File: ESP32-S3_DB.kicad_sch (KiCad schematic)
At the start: 0 parts

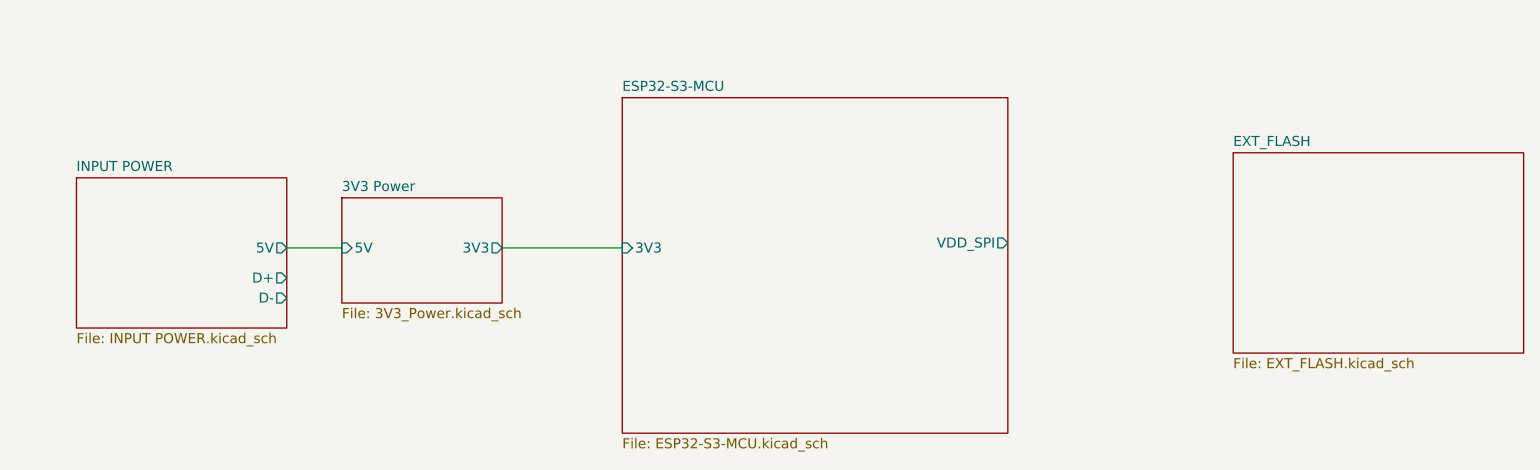
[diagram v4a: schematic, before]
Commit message: Added USB-To-UART Converter
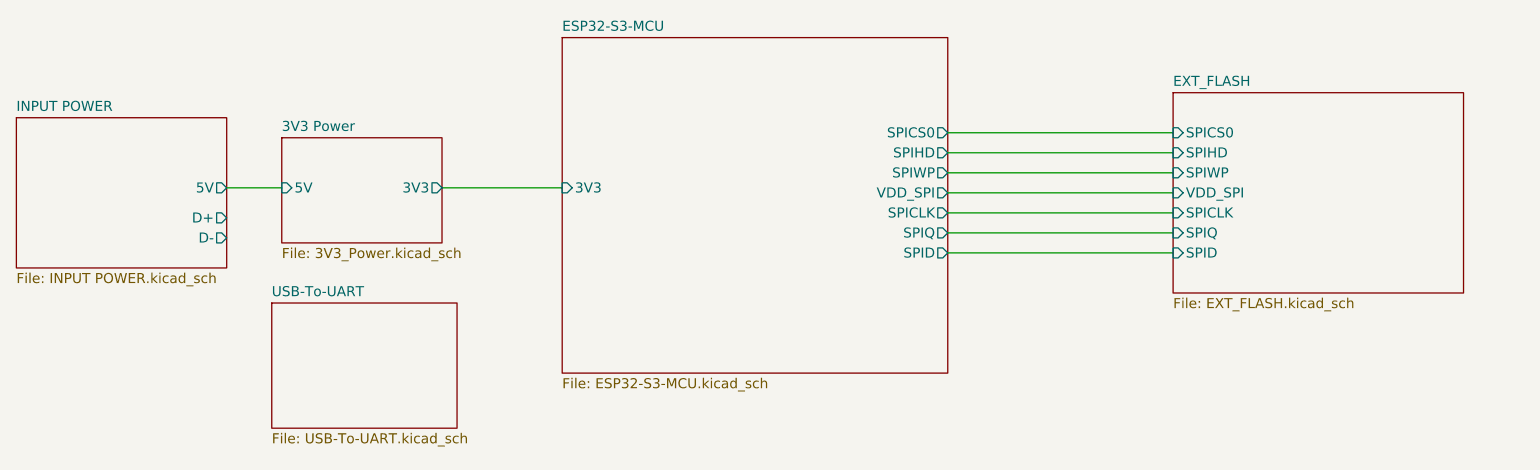
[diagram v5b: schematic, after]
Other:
- added sheet USB-To-UART (USB-To-UART.kicad_sch)
- sheet ESP32-S3-MCU ports: added SPICLK, SPICS0, SPID, SPIHD, SPIQ, SPIWP; removed none
- sheet EXT_FLASH ports: added SPICLK, SPICS0, SPID, SPIHD, SPIQ, SPIWP, VDD_SPI; removed none
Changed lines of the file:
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@@
 (kicad_sch (version 20230121) (generator eeschema)
   (paper "A4")
-  (wire (pts (xy 90.17 96.52) (xy 97.155 96.52))
+  (wire (pts (xy 173.99 97.155) (xy 202.565 97.155))
     (stroke (width 0) (type default))
   )
-  (wire (pts (xy 117.475 96.52) (xy 132.715 96.52))
+  (wire (pts (xy 173.99 92.075) (xy 202.565 92.075))
     (stroke (width 0) (type default))
   )
-  (sheet (at 210.185 84.455) (size 36.83 25.4) (fields_autoplaced)
+  (wire (pts (xy 173.99 94.615) (xy 202.565 94.615))
+    (stroke (width 0) (type default))
+  )
+  (wire (pts (xy 173.99 86.995) (xy 202.565 86.995))
+    (stroke (width 0) (type default))
+  )
+  (wire (pts (xy 173.99 89.535) (xy 202.565 89.535))
+    (stroke (width 0) (type default))
+  )
+  (wire (pts (xy 173.99 84.455) (xy 202.565 84.455))
+    (stroke (width 0) (type default))
+  )
+  (wire (pts (xy 82.55 88.9) (xy 89.535 88.9))
+    (stroke (width 0) (type default))
+  )
+  (wire (pts (xy 173.99 81.915) (xy 202.565 81.915))
+    (stroke (width 0) (type default))
+  )
+  (wire (pts (xy 109.855 88.9) (xy 125.095 88.9))
+    (stroke (width 0) (type default))
+  )
+  (sheet (at 202.565 76.835) (size 36.83 25.4) (fields_autoplaced)
     (stroke (width 0.1524) (type solid))
     (fill (color 255 255 194 1.0000))
-    (property "Sheetname" "EXT_FLASH" (at 210.185 83.7434 0)
+    (property "Sheetname" "EXT_FLASH" (at 202.565 76.1234 0)
       (effects (font (size 1.27 1.27)) (justify left bottom))
     )
-    (property "Sheetfile" "EXT_FLASH.kicad_sch" (at 210.185 110.4396 0)
+    (property "Sheetfile" "EXT_FLASH.kicad_sch" (at 202.565 102.8196 0)
       (effects (font (size 1.27 1.27)) (justify left top))
+    )
+    (pin "SPIHD" input (at 202.565 84.455 180)
+      (effects (font (size 1.27 1.27)) (justify left))
+    )
+    (pin "SPIWP" input (at 202.565 86.995 180)
+      (effects (font (size 1.27 1.27)) (justify left))
+    )
+    (pin "VDD_SPI" input (at 202.565 89.535 180)
+      (effects (font (size 1.27 1.27)) (justify left))
+    )
+    (pin "SPIQ" input (at 202.565 94.615 180)
+      (effects (font (size 1.27 1.27)) (justify left))
+    )
+    (pin "SPICLK" input (at 202.565 92.075 180)
+      (effects (font (size 1.27 1.27)) (justify left))
+    )
+    (pin "SPICS0" input (at 202.565 81.915 180)
+      (effects (font (size 1.27 1.27)) (justify left))
+    )
+    (pin "SPID" input (at 202.565 97.155 180)
+      (effects (font (size 1.27 1.27)) (justify left))
     )
     (instances
@@
     )
   )
-  (sheet (at 63.5 87.63) (size 26.67 19.05) (fields_autoplaced)
+  (sheet (at 55.88 80.01) (size 26.67 19.05) (fields_autoplaced)
     (stroke (width 0.1524) (type solid))
     (fill (color 255 255 194 1.0000))
-    (property "Sheetname" "INPUT POWER" (at 63.5 86.9184 0)
+    (property "Sheetname" "INPUT POWER" (at 55.88 79.2984 0)
       (effects (font (size 1.27 1.27)) (justify left bottom))
     )
-    (property "Sheetfile" "INPUT POWER.kicad_sch" (at 63.5 107.2646 0)
+    (property "Sheetfile" "INPUT POWER.kicad_sch" (at 55.88 99.6446 0)
       (effects (font (size 1.27 1.27)) (justify left top))
     )
-    (pin "D-" output (at 90.17 102.87 0)
+    (pin "D-" output (at 82.55 95.25 0)
       (effects (font (size 1.27 1.27)) (justify right))
     )
-    (pin "D+" output (at 90.17 100.33 0)
+    (pin "D+" output (at 82.55 92.71 0)
       (effects (font (size 1.27 1.27)) (justify right))
     )
-    (pin "5V" output (at 90.17 96.52 0)
+    (pin "5V" output (at 82.55 88.9 0)
       (effects (font (size 1.27 1.27)) (justify right))
     )
@@
     )
   )
-  (sheet (at 132.715 77.47) (size 48.895 42.545) (fields_autoplaced)
+  (sheet (at 88.265 103.505) (size 23.495 15.875) (fields_autoplaced)
     (stroke (width 0.1524) (type solid))
     (fill (color 255 255 194 1.0000))
-    (property "Sheetname" "ESP32-S3-MCU" (at 132.715 76.7584 0)
+    (property "Sheetname" "USB-To-UART" (at 88.265 102.7934 0)
       (effects (font (size 1.27 1.27)) (justify left bottom))
     )
-    (property "Sheetfile" "ESP32-S3-MCU.kicad_sch" (at 132.715 120.5996 0)
+    (property "Sheetfile" "USB-To-UART.kicad_sch" (at 88.265 119.9646 0)
       (effects (font (size 1.27 1.27)) (justify left top))
     )
-    (pin "3V3" input (at 132.715 96.52 180)
+    (instances
+      (project "ESP32-S3_DB"
+        (path "/b7fc4bd3-c219-4455-832b-8d795385dcf1" (page "6"))
+      )
+    )
+  )
+  (sheet (at 125.095 69.85) (size 48.895 42.545) (fields_autoplaced)
+    (stroke (width 0.1524) (type solid))
+    (fill (color 255 255 194 1.0000))
+    (property "Sheetname" "ESP32-S3-MCU" (at 125.095 69.1384 0)
+      (effects (font (size 1.27 1.27)) (justify left bottom))
+    )
+    (property "Sheetfile" "ESP32-S3-MCU.kicad_sch" (at 125.095 112.9796 0)
+      (effects (font (size 1.27 1.27)) (justify left top))
+    )
+    (pin "3V3" input (at 125.095 88.9 180)
       (effects (font (size 1.27 1.27)) (justify left))
     )
-    (pin "VDD_SPI" output (at 181.61 95.885 0)
+    (pin "VDD_SPI" output (at 173.99 89.535 0)
+      (effects (font (size 1.27 1.27)) (justify right))
+    )
+    (pin "SPIWP" output (at 173.99 86.995 0)
+      (effects (font (size 1.27 1.27)) (justify right))
+    )
+    (pin "SPIHD" output (at 173.99 84.455 0)
+      (effects (font (size 1.27 1.27)) (justify right))
+    )
+    (pin "SPICS0" output (at 173.99 81.915 0)
+      (effects (font (size 1.27 1.27)) (justify right))
+    )
+    (pin "SPICLK" output (at 173.99 92.075 0)
+      (effects (font (size 1.27 1.27)) (justify right))
+    )
+    (pin "SPIQ" output (at 173.99 94.615 0)
+      (effects (font (size 1.27 1.27)) (justify right))
+    )
+    (pin "SPID" output (at 173.99 97.155 0)
       (effects (font (size 1.27 1.27)) (justify right))
     )
@@
     )
   )
-  (sheet (at 97.155 90.17) (size 20.32 13.335) (fields_autoplaced)
+  (sheet (at 89.535 82.55) (size 20.32 13.335) (fields_autoplaced)
     (stroke (width 0.1524) (type solid))
     (fill (color 255 255 194 1.0000))
-    (property "Sheetname" "3V3 Power" (at 97.155 89.4584 0)
+    (property "Sheetname" "3V3 Power" (at 89.535 81.8384 0)
       (effects (font (size 1.27 1.27)) (justify left bottom))
     )
-    (property "Sheetfile" "3V3_Power.kicad_sch" (at 97.155 104.0896 0)
+    (property "Sheetfile" "3V3_Power.kicad_sch" (at 89.535 96.4696 0)
       (effects (font (size 1.27 1.27)) (justify left top))
     )
-    (pin "3V3" output (at 117.475 96.52 0)
+    (pin "3V3" output (at 109.855 88.9 0)
       (effects (font (size 1.27 1.27)) (justify right))
     )
-    (pin "5V" input (at 97.155 96.52 180)
+    (pin "5V" input (at 89.535 88.9 180)
       (effects (font (size 1.27 1.27)) (justify left))
     )

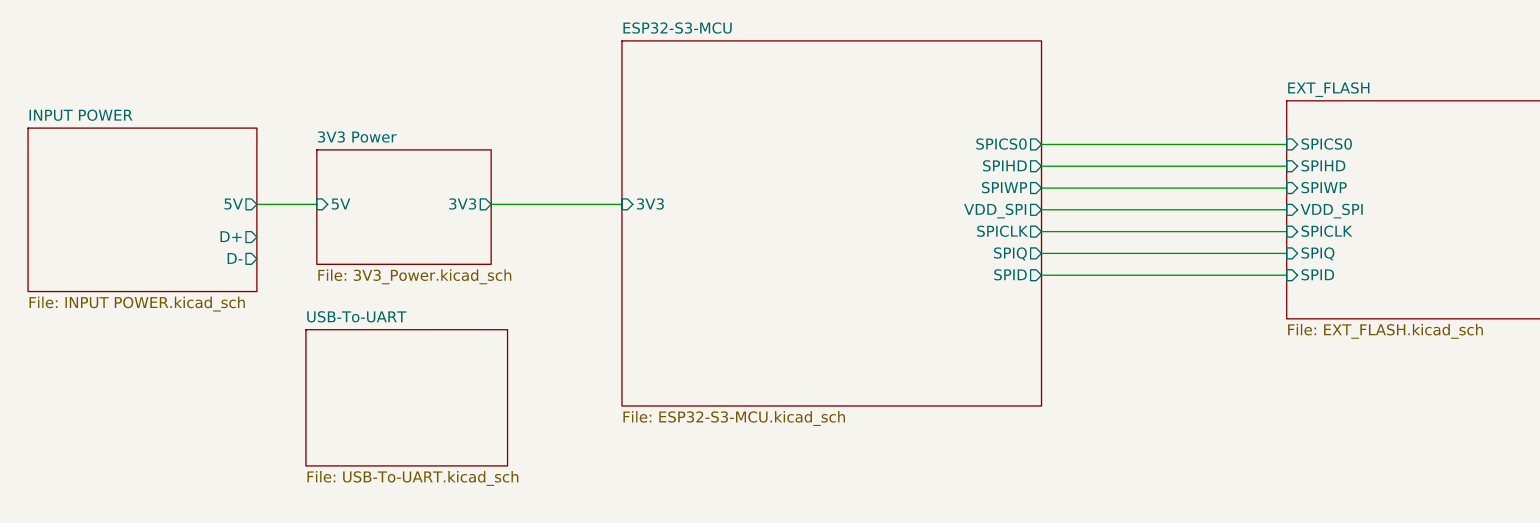
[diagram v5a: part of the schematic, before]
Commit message: Made USB-To-UART connections
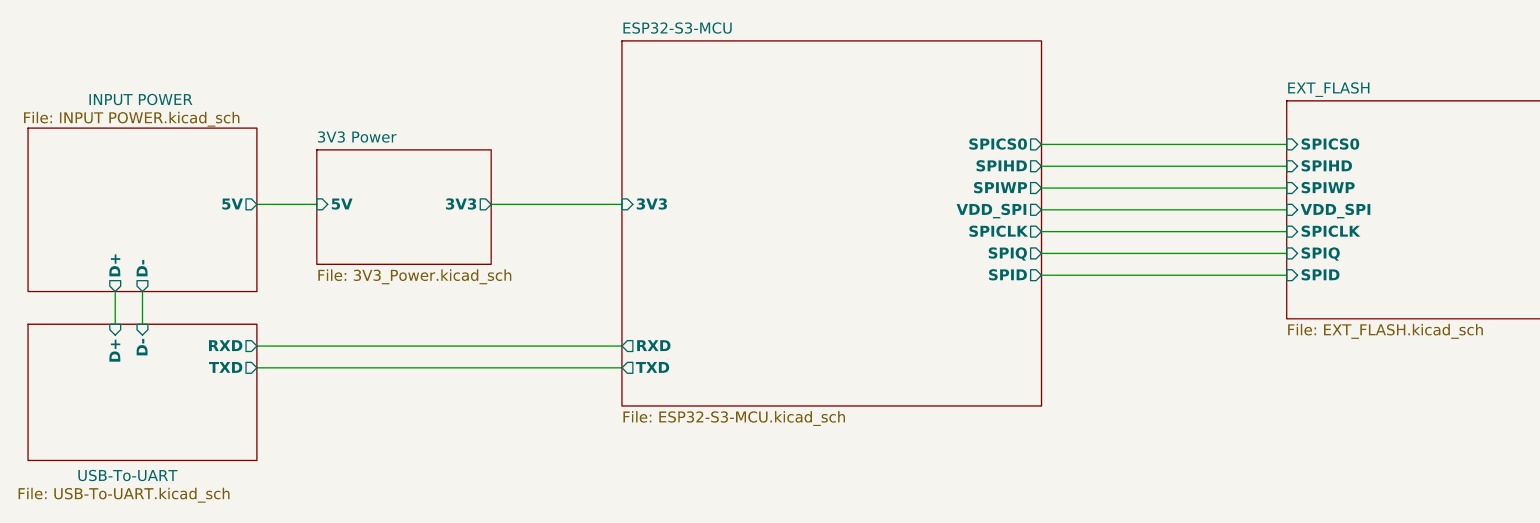
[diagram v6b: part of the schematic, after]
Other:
- sheet ESP32-S3-MCU ports: added RXD, TXD; removed none
- sheet USB-To-UART ports: added D+, D-, RXD, TXD; removed none
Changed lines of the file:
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@@
+    (stroke (width 0) (type default))
+  )
+  (wire (pts (xy 66.04 99.06) (xy 66.04 102.87))
+    (stroke (width 0) (type default))
+  )
+  (wire (pts (xy 69.215 99.06) (xy 69.215 102.87))
     (stroke (width 0) (type default))
   )
@@
     (stroke (width 0) (type default))
   )
+  (wire (pts (xy 82.55 105.41) (xy 125.095 105.41))
+    (stroke (width 0) (type default))
+  )
   (wire (pts (xy 173.99 81.915) (xy 202.565 81.915))
     (stroke (width 0) (type default))
@@
     (stroke (width 0) (type default))
   )
+  (wire (pts (xy 82.55 107.95) (xy 125.095 107.95))
+    (stroke (width 0) (type default))
+  )
   (sheet (at 202.565 76.835) (size 36.83 25.4) (fields_autoplaced)
-    (stroke (width 0.1524) (type solid))
+    (stroke (width 0.1524) (type solid) (color 0 0 0 1))
     (fill (color 255 255 194 1.0000))
     (property "Sheetname" "EXT_FLASH" (at 202.565 76.1234 0)
@@
     )
     (pin "SPIHD" input (at 202.565 84.455 180)
-      (effects (font (size 1.27 1.27)) (justify left))
+      (effects (font (size 1.27 1.27) (thickness 0.254) bold (color 0 0 255 1)) (justify left))
     )
     (pin "SPIWP" input (at 202.565 86.995 180)
-      (effects (font (size 1.27 1.27)) (justify left))
+      (effects (font (size 1.27 1.27) (thickness 0.254) bold (color 0 0 255 1)) (justify left))
     )
     (pin "VDD_SPI" input (at 202.565 89.535 180)
-      (effects (font (size 1.27 1.27)) (justify left))
+      (effects (font (size 1.27 1.27) (thickness 0.254) bold (color 0 0 255 1)) (justify left))
     )
     (pin "SPIQ" input (at 202.565 94.615 180)
-      (effects (font (size 1.27 1.27)) (justify left))
+      (effects (font (size 1.27 1.27) (thickness 0.254) bold (color 0 0 255 1)) (justify left))
     )
     (pin "SPICLK" input (at 202.565 92.075 180)
-      (effects (font (size 1.27 1.27)) (justify left))
+      (effects (font (size 1.27 1.27) (thickness 0.254) bold (color 0 0 255 1)) (justify left))
     )
     (pin "SPICS0" input (at 202.565 81.915 180)
-      (effects (font (size 1.27 1.27)) (justify left))
+      (effects (font (size 1.27 1.27) (thickness 0.254) bold (color 0 0 255 1)) (justify left))
     )
     (pin "SPID" input (at 202.565 97.155 180)
-      (effects (font (size 1.27 1.27)) (justify left))
+      (effects (font (size 1.27 1.27) (thickness 0.254) bold (color 0 0 255 1)) (justify left))
     )
     (instances
@@
     )
   )
-  (sheet (at 55.88 80.01) (size 26.67 19.05) (fields_autoplaced)
-    (stroke (width 0.1524) (type solid))
+  (sheet (at 55.88 80.01) (size 26.67 19.05)
+    (stroke (width 0.1524) (type solid) (color 0 0 0 1))
     (fill (color 255 255 194 1.0000))
-    (property "Sheetname" "INPUT POWER" (at 55.88 79.2984 0)
+    (property "Sheetname" "INPUT POWER" (at 62.865 77.47 0)
       (effects (font (size 1.27 1.27)) (justify left bottom))
     )
-    (property "Sheetfile" "INPUT POWER.kicad_sch" (at 55.88 99.6446 0)
+    (property "Sheetfile" "INPUT POWER.kicad_sch" (at 55.245 78.105 0)
       (effects (font (size 1.27 1.27)) (justify left top))
     )
-    (pin "D-" output (at 82.55 95.25 0)
-      (effects (font (size 1.27 1.27)) (justify right))
+    (pin "D-" output (at 69.215 99.06 270)
+      (effects (font (size 1.27 1.27) (thickness 0.254) bold (color 0 0 255 1)) (justify left))
     )
-    (pin "D+" output (at 82.55 92.71 0)
-      (effects (font (size 1.27 1.27)) (justify right))
+    (pin "D+" output (at 66.04 99.06 270)
+      (effects (font (size 1.27 1.27) (thickness 0.254) bold (color 0 0 255 1)) (justify left))
     )
     (pin "5V" output (at 82.55 88.9 0)
-      (effects (font (size 1.27 1.27)) (justify right))
+      (effects (font (size 1.27 1.27) (thickness 0.254) bold (color 255 0 0 1)) (justify right))
     )
     (instances
@@
     )
   )
-  (sheet (at 88.265 103.505) (size 23.495 15.875) (fields_autoplaced)
-    (stroke (width 0.1524) (type solid))
+  (sheet (at 55.88 102.87) (size 26.67 15.875)
+    (stroke (width 0.1524) (type solid) (color 0 0 0 1))
     (fill (color 255 255 194 1.0000))
-    (property "Sheetname" "USB-To-UART" (at 88.265 102.7934 0)
+    (property "Sheetname" "USB-To-UART" (at 61.595 121.285 0)
       (effects (font (size 1.27 1.27)) (justify left bottom))
     )
-    (property "Sheetfile" "USB-To-UART.kicad_sch" (at 88.265 119.9646 0)
+    (property "Sheetfile" "USB-To-UART.kicad_sch" (at 54.61 121.92 0)
       (effects (font (size 1.27 1.27)) (justify left top))
+    )
+    (pin "D+" input (at 66.04 102.87 90)
+      (effects (font (size 1.27 1.27) (thickness 0.254) bold (color 0 0 255 1)) (justify right))
+    )
+    (pin "D-" input (at 69.215 102.87 90)
+      (effects (font (size 1.27 1.27) (thickness 0.254) bold (color 0 0 255 1)) (justify right))
+    )
+    (pin "RXD" output (at 82.55 105.41 0)
+      (effects (font (size 1.27 1.27) (thickness 0.254) bold (color 0 0 255 1)) (justify right))
+    )
+    (pin "TXD" output (at 82.55 107.95 0)
+      (effects (font (size 1.27 1.27) (thickness 0.254) bold (color 0 0 255 1)) (justify right))
     )
     (instances
@@
   )
   (sheet (at 125.095 69.85) (size 48.895 42.545) (fields_autoplaced)
-    (stroke (width 0.1524) (type solid))
+    (stroke (width 0.1524) (type solid) (color 0 0 0 1))
     (fill (color 255 255 194 1.0000))
     (property "Sheetname" "ESP32-S3-MCU" (at 125.095 69.1384 0)
@@
     )
     (pin "3V3" input (at 125.095 88.9 180)
-      (effects (font (size 1.27 1.27)) (justify left))
+      (effects (font (size 1.27 1.27) (thickness 0.254) bold (color 255 0 0 1)) (justify left))
     )
     (pin "VDD_SPI" output (at 173.99 89.535 0)
-      (effects (font (size 1.27 1.27)) (justify right))
+      (effects (font (size 1.27 1.27) (thickness 0.254) bold (color 0 0 255 1)) (justify right))
     )
     (pin "SPIWP" output (at 173.99 86.995 0)
-      (effects (font (size 1.27 1.27)) (justify right))
+      (effects (font (size 1.27 1.27) (thickness 0.254) bold (color 0 0 255 1)) (justify right))
     )
     (pin "SPIHD" output (at 173.99 84.455 0)
-      (effects (font (size 1.27 1.27)) (justify right))
+      (effects (font (size 1.27 1.27) (thickness 0.254) bold (color 0 0 255 1)) (justify right))
     )
     (pin "SPICS0" output (at 173.99 81.915 0)
-      (effects (font (size 1.27 1.27)) (justify right))
+      (effects (font (size 1.27 1.27) (thickness 0.254) bold (color 0 0 255 1)) (justify right))
     )
     (pin "SPICLK" output (at 173.99 92.075 0)
-      (effects (font (size 1.27 1.27)) (justify right))
+      (effects (font (size 1.27 1.27) (thickness 0.254) bold (color 0 0 255 1)) (justify right))
     )
     (pin "SPIQ" output (at 173.99 94.615 0)
-      (effects (font (size 1.27 1.27)) (justify right))
+      (effects (font (size 1.27 1.27) (thickness 0.254) bold (color 0 0 255 1)) (justify right))
     )
     (pin "SPID" output (at 173.99 97.155 0)
-      (effects (font (size 1.27 1.27)) (justify right))
+      (effects (font (size 1.27 1.27) (thickness 0.254) bold (color 0 0 255 1)) (justify right))
+    )
+    (pin "TXD" output (at 125.095 107.95 180)
+      (effects (font (size 1.27 1.27) (thickness 0.254) bold (color 0 0 255 1)) (justify left))
+    )
+    (pin "RXD" output (at 125.095 105.41 180)
+      (effects (font (size 1.27 1.27) (thickness 0.254) bold (color 0 0 255 1)) (justify left))
     )
     (instances
@@
   )
   (sheet (at 89.535 82.55) (size 20.32 13.335) (fields_autoplaced)
-    (stroke (width 0.1524) (type solid))
+    (stroke (width 0.1524) (type solid) (color 0 0 0 1))
     (fill (color 255 255 194 1.0000))
     (property "Sheetname" "3V3 Power" (at 89.535 81.8384 0)
@@
     )
     (pin "3V3" output (at 109.855 88.9 0)
-      (effects (font (size 1.27 1.27)) (justify right))
+      (effects (font (size 1.27 1.27) (thickness 0.254) bold (color 255 0 0 1)) (justify right))
     )
     (pin "5V" input (at 89.535 88.9 180)
-      (effects (font (size 1.27 1.27)) (justify left))
+      (effects (font (size 1.27 1.27) (thickness 0.254) bold (color 255 0 0 1)) (justify left))
     )
     (instances
